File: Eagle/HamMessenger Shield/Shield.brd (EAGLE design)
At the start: 100 x 80 mm, 22 parts, among them J2 KEYBOARD GROVE, Q1 2N7000

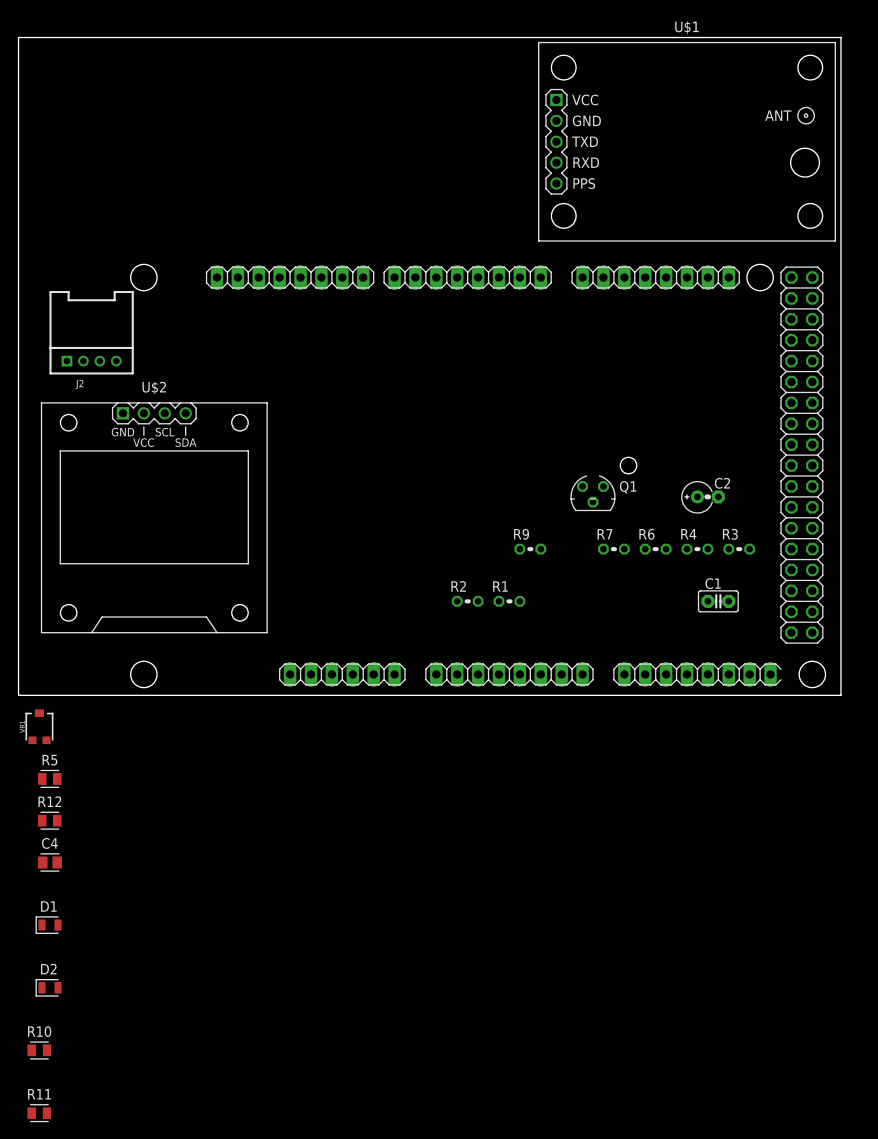
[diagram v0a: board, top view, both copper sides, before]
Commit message: Continue work on PCB. Update schematic.
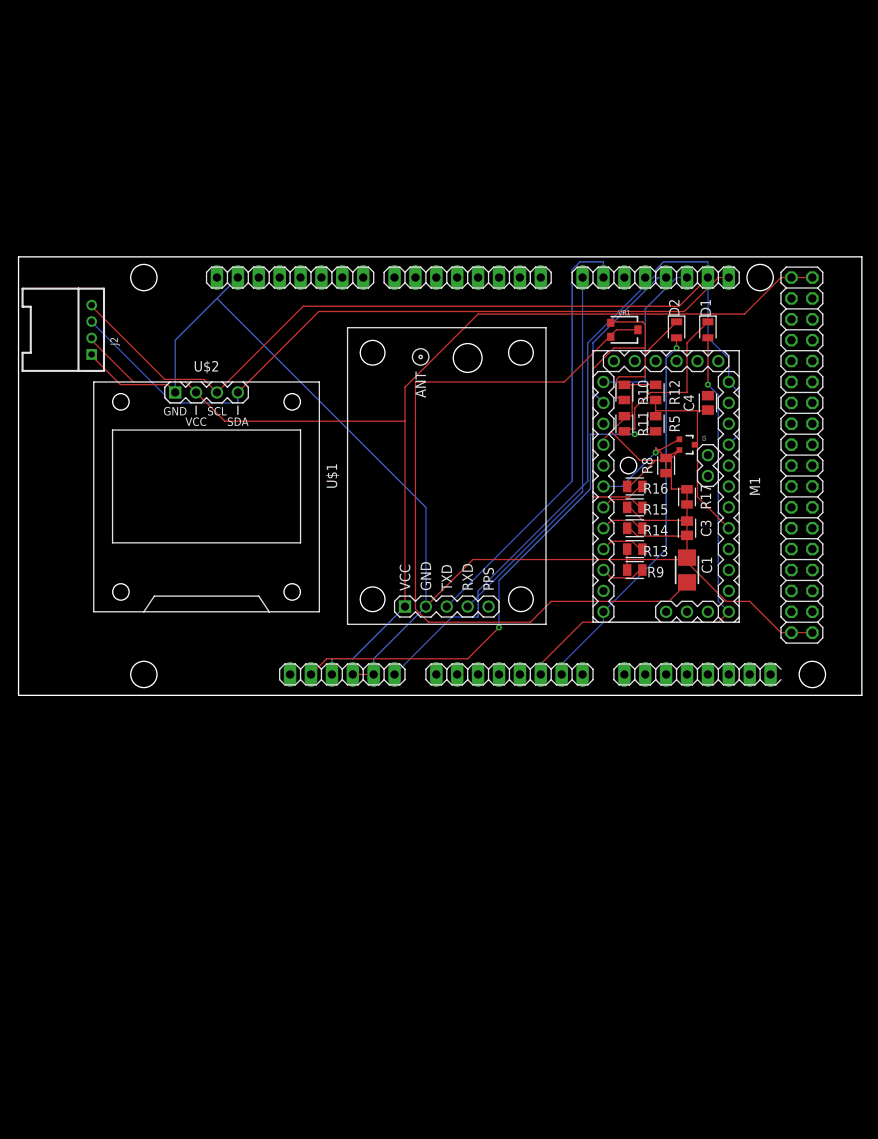
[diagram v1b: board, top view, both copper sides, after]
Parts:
- removed C2: 4.7uF, resistor:E2,5-4R
- removed Q1: 2N7000, transistor-fet-edited:TO92_MOD
- removed R1, R6: 1k, resistor:0204V
- removed R2: 2k2, resistor:0204V
- removed R3: 3k9, resistor:0204V
- removed R4: 8k2, resistor:0204V
- removed R7: 270, resistor:0204V
- added C3: 100nf, Capacitor:CAPC2012X110
- added M1: ARDUINO-PRO-MINI-3.3V, diy-modules:ARDUINO-PRO-MINI
- added Q3: MOSFET-NCHANNEL2N7002PW, BeagleBone_Blue_R3:SOT323
- added R13: 2k2, Resistor:RESC2012X65
- added R14: 3k9, Resistor:RESC2012X65
- added R15: 8k2, Resistor:RESC2012X65
- added R16: 1k, Resistor:RESC2012X65
- added R17: 270, Resistor:RESC2012X65
- added R8: 10k, Resistor:RESC2012X65
- C1: value 100nF -> 4.7uf; device capacitor-wima:C2.5-2 -> adafruit:CT3528
- R9: value 10k -> 1k; device rcl:0204V -> Resistor:RESC2012X65
- moved D2 110.5 mm to (80.0, 44.5), turned to 270 degrees
- moved R11 109.9 mm to (73.7, 33.0), turned to 270 degrees
- moved D1 107.9 mm to (83.8, 44.5), turned to 270 degrees
- moved R10 107.0 mm to (73.7, 36.8), turned to 270 degrees
- moved C4 97.6 mm to (83.8, 35.6), turned to 90 degrees
- moved R12 90.2 mm to (77.5, 36.8), turned to 270 degrees
- moved VR1 85.9 mm to (73.7, 44.5), turned to 270 degrees
- moved R5 85.4 mm to (77.5, 33.0), turned to 270 degrees
- moved U$1 50.0 mm to (52.1, 26.7), turned to 90 degrees
- moved R9 13.0 mm to (74.9, 15.2)
- moved U$2 6.84 mm to (22.9, 24.1)
- moved C1 5.39 mm to (81.3, 15.2), turned to 270 degrees
- moved J2 3.81 mm to (8.89, 44.5), turned to 90 degrees
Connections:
- removed net +VIN: IC1.6
- removed net RXD: U$1.4
- new net GND.2: M1.J6.2
- new net RX_GPS: IC1.29, U$1.3
- new net RX_MODEM: IC1.25, M1.J7.12
- new net TX_GPS: IC1.30, U$1.4
- new net TX_MODEM: IC1.26, M1.J7.11
- new net VCC: IC1.6, M1.J6.1, M1.J6.4
- net A0: now also M1.J6.8
- net D10: now also IC1.12, M1.J6.12
- net D3: now also M1.J7.7, Q3.1, R8.2; no longer Q1.2, R9.1
- net D4: now also M1.J7.6, R15.2; no longer R4.1
- net D5: now also M1.J7.5, R14.2; no longer R3.1
- net D6: now also M1.J7.4, R13.2; no longer R2.1
- net D7: now also M1.J7.3, R9.2; no longer R1.1
- net D9: now also IC1.13, M1.J7.1
- net GND: now also C1.-, C3.1, C3.2, M1.J7.9, Q3.2, R13.1, R14.1, R15.1, R16.1, R17.1, R17.2, R8.1, R9.1; no longer C1.1, C1.2, C2.-, Q1.3, R1.2, R2.2, R3.2, R4.2, R6.1, R7.1, R7.2, R9.2
- net LINE_LEVEL_OUT: now also C1.+; no longer C2.+
- net MIC_LEVEL_OUT: now also R16.2; no longer R6.2
- net PTT_V+: now also Q3.3; no longer Q1.1
- net SCL: now also IC1.24
- net SDA: now also IC1.23
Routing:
- net GND: track 0.00 -> 208.5 mm
- net +5V: track 0.00 -> 137.6 mm
- net VCC: track 0.00 -> 95.3 mm
- net LINE_LEVEL_OUT: track 0.00 -> 93.1 mm
- net SDA: track 0.00 -> 88.8 mm
- net SCL: track 0.00 -> 85.2 mm
- net +3V3: track 0.00 -> 61.4 mm, vias 0 -> 2
- net D10: track 0.00 -> 61.1 mm, vias 0 -> 1
- net RX_GPS: track 0.00 -> 53.4 mm
- net D9: track 0.00 -> 46.7 mm, vias 0 -> 1
- net TX_GPS: track 0.00 -> 45.8 mm
- net MIC_LEVEL_OUT: track 0.00 -> 36.7 mm
- net A0: track 0.00 -> 24.3 mm
- net N$4: track 0.00 -> 20.9 mm
- net RX_MODEM: track 0.00 -> 20.6 mm
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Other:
- board size 100 x 80 mm -> 102.5 x 53.3 mm

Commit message: Net re-routing
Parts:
- moved R8 1.27 mm to (78.7, 26.7)
- moved Q3 1.27 mm to (80.0, 30.5), turned to 0 degrees
- turned R16 to 180 degrees
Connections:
- new net N$2: C1.-, C3.1, R13.1, R14.1, R15.1, R17.2, R9.1
- net GND: no longer C1.-, C3.1, R13.1, R14.1, R15.1, R17.2, R9.1
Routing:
- net N$2: track 0.00 -> 21.8 mm
- net GND: track 208.5 -> 187.1 mm
- net MIC_LEVEL_OUT: track 36.7 -> 32.3 mm
- net VCC: track 95.3 -> 97.3 mm
- net D3: track 13.7 -> 15.3 mm
- net RX_MODEM: track 20.6 -> 19.9 mm
- net TX_MODEM: track 20.0 -> 19.4 mm

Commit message: PCB Updates
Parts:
- added J3: (no value), Wurth_Connectors_WR-TBL Rising Cage Clamp:691210910004
- moved R13 1.27 mm to (74.9, 16.5), turned to 180 degrees
- moved R14 1.27 mm to (74.9, 19.1), turned to 180 degrees
- moved R15 1.27 mm to (74.9, 21.6), turned to 180 degrees
- moved R9 1.27 mm to (74.9, 14.0), turned to 180 degrees
- moved R16 1.02 mm to (74.9, 24.4)
- turned R10 to 90 degrees
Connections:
- net GND: now also J3.1
- net LINE_LEVEL_IN: now also J3.4
- net MIC_LEVEL_OUT: now also J3.3
- net PTT_V+: now also J3.2
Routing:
- net LINE_LEVEL_IN: track 0.00 -> 121.8 mm, vias 0 -> 4
- net PTT_V+: track 0.00 -> 96.9 mm, vias 0 -> 3
- net MIC_LEVEL_OUT: track 32.3 -> 121.2 mm, vias 0 -> 4
- net VCC: track 97.3 -> 82.2 mm, vias 0 -> 2
- net GND: track 187.1 -> 181.6 mm
- net RX_GPS: track 53.4 -> 48.9 mm, vias 0 -> 1
- net N$3: track 15.4 -> 11.2 mm
- net D9: track 46.7 -> 50.4 mm
- net D7: track 5.52 -> 3.42 mm
- net D6: track 5.52 -> 3.42 mm
- net D5: track 5.52 -> 3.42 mm
- net D4: track 5.52 -> 3.42 mm
- net +3V3: track 61.4 -> 62.7 mm
- net N$2: track 21.8 -> 22.9 mm
- net SDA: track 88.8 -> 89.7 mm, vias 0 -> 1
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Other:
- board size 102.5 x 53.3 mm -> 101.6 x 53.3 mm

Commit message: Add ground plane
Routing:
- net MIC_LEVEL_OUT: track 121.2 -> 118.0 mm
- net GND: vias 0 -> 6
- added copper zone on layer 1, net GND
- added copper zone on layer 16, net GND
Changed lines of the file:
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@@
 <wire x1="17.78" y1="21.844" x2="45.974" y2="21.844" width="0.1524" layer="16"/>
 <via x="45.974" y="21.844" extent="1-16" drill="0.35"/>
-<wire x1="45.974" y1="21.844" x2="45.974" y2="29.972" width="0.1524" layer="1"/>
-<via x="45.974" y="29.972" extent="1-16" drill="0.35"/>
-<wire x1="45.974" y1="29.972" x2="65.532" y2="29.972" width="0.1524" layer="16"/>
-<via x="65.532" y="29.972" extent="1-16" drill="0.35"/>
-<wire x1="65.532" y1="29.972" x2="68.834" y2="26.67" width="0.1524" layer="1"/>
-<wire x1="68.834" y1="26.67" x2="68.834" y2="23.114" width="0.1524" layer="1"/>
+<wire x1="45.974" y1="21.844" x2="45.974" y2="28.194" width="0.1524" layer="1"/>
+<via x="45.974" y="28.194" extent="1-16" drill="0.35"/>
+<wire x1="65.278" y1="28.194" x2="45.974" y2="28.194" width="0.1524" layer="16"/>
+<wire x1="65.278" y1="28.194" x2="65.532" y2="28.448" width="0.1524" layer="16"/>
+<via x="65.532" y="28.448" extent="1-16" drill="0.35"/>
+<wire x1="65.532" y1="28.448" x2="68.834" y2="25.146" width="0.1524" layer="1"/>
+<wire x1="68.834" y1="25.146" x2="68.834" y2="23.114" width="0.1524" layer="1"/>
 <via x="68.834" y="23.114" extent="1-16" drill="0.35"/>
 <wire x1="68.834" y1="23.114" x2="70.104" y2="24.384" width="0.1524" layer="16"/>
@@
 <wire x1="4.572" y1="13.716" x2="19.05" y2="28.194" width="0.1524" layer="1"/>
 <wire x1="19.05" y1="28.194" x2="19.05" y2="36.83" width="0.1524" layer="1"/>
-<wire x1="81.28" y1="19.6723" x2="81.28" y2="19.4446" width="0" layer="19" extent="1-1"/>
-<wire x1="49.53" y1="10.795" x2="71.12" y2="30.48" width="0" layer="19" extent="1-1"/>
+<polygon width="0.1524" layer="1" isolate="0.4064">
+<vertex x="0" y="53.34"/>
+<vertex x="0" y="0"/>
+<vertex x="101.6" y="0"/>
+<vertex x="101.6" y="53.34"/>
+</polygon>
+<polygon width="0.1524" layer="16" isolate="0.4064">
+<vertex x="0" y="53.34"/>
+<vertex x="101.6" y="53.34"/>
+<vertex x="101.6" y="0"/>
+<vertex x="0" y="0"/>
+</polygon>
+<via x="38.608" y="41.148" extent="1-16" drill="0.35"/>
+<via x="65.786" y="42.418" extent="1-16" drill="0.35"/>
+<via x="65.024" y="14.732" extent="1-16" drill="0.35"/>
+<via x="66.04" y="8.636" extent="1-16" drill="0.35"/>
+<via x="74.93" y="10.16" extent="1-16" drill="0.35"/>
+<via x="80.518" y="35.814" extent="1-16" drill="0.35"/>
 </signal>
 <signal name="D3">
@@
 <contactref element="U$1" pad="1"/>
 <contactref element="U$2" pad="2"/>
-<wire x1="13.97" y1="38.1" x2="8.89" y2="43.18" width="0.1524" layer="1"/>
-<wire x1="20.32" y1="38.1" x2="13.97" y2="38.1" width="0.1524" layer="1"/>
-<wire x1="21.59" y1="36.83" x2="20.32" y2="38.1" width="0.1524" layer="1"/>
+<wire x1="13.716" y1="38.354" x2="8.89" y2="43.18" width="0.1524" layer="1"/>
+<wire x1="20.066" y1="38.354" x2="13.716" y2="38.354" width="0.1524" layer="1"/>
+<wire x1="21.59" y1="36.83" x2="20.066" y2="38.354" width="0.1524" layer="1"/>
 <wire x1="8.89" y1="43.18" x2="8.89" y2="43.45" width="0.1524" layer="1"/>
 <wire x1="96.52" y1="50.8" x2="93.98" y2="50.8" width="0.1524" layer="1"/>
@@
 <contactref element="U$2" pad="3"/>
 <contactref element="IC1" pad="24"/>
-<wire x1="17.78" y1="38.4175" x2="8.89" y2="47.3075" width="0.1524" layer="1"/>
-<wire x1="22.5425" y1="38.4175" x2="17.78" y2="38.4175" width="0.1524" layer="1"/>
-<wire x1="24.13" y1="36.83" x2="22.5425" y2="38.4175" width="0.1524" layer="1"/>
-<wire x1="8.89" y1="47.3075" x2="8.89" y2="47.45" width="0.1524" layer="1"/>
+<wire x1="8.89" y1="47.45" x2="11.0335" y2="47.45" width="0.1524" layer="1"/>
+<wire x1="18.034" y1="40.4495" x2="11.0335" y2="47.45" width="0.1524" layer="1"/>
+<wire x1="20.5105" y1="40.4495" x2="18.034" y2="40.4495" width="0.1524" layer="1"/>
+<wire x1="24.13" y1="36.83" x2="20.5105" y2="40.4495" width="0.1524" layer="1"/>
 <wire x1="24.13" y1="36.83" x2="34.544" y2="47.244" width="0.1524" layer="1"/>
 <wire x1="34.544" y1="47.244" x2="79.756" y2="47.244" width="0.1524" layer="1"/>
@@
 <wire x1="85.09" y1="11.43" x2="85.09" y2="36.5125" width="0.1524" layer="16"/>
 <wire x1="86.36" y1="10.16" x2="85.09" y2="11.43" width="0.1524" layer="16"/>
-<wire x1="68.58" y1="8.89" x2="63.5" y2="3.81" width="0.1524" layer="1"/>
-<wire x1="63.5" y1="3.81" x2="63.5" y2="2.54" width="0.1524" layer="1"/>
-<wire x1="85.09" y1="8.89" x2="68.58" y2="8.89" width="0.1524" layer="1"/>
+<wire x1="68.072" y1="8.89" x2="63.5" y2="4.318" width="0.1524" layer="1"/>
+<wire x1="63.5" y1="4.318" x2="63.5" y2="2.54" width="0.1524" layer="1"/>
+<wire x1="85.09" y1="8.89" x2="68.072" y2="8.89" width="0.1524" layer="1"/>
 <wire x1="86.36" y1="10.16" x2="85.09" y2="8.89" width="0.1524" layer="1"/>
 <via x="83.82" y="37.7825" extent="1-16" drill="0.35"/>

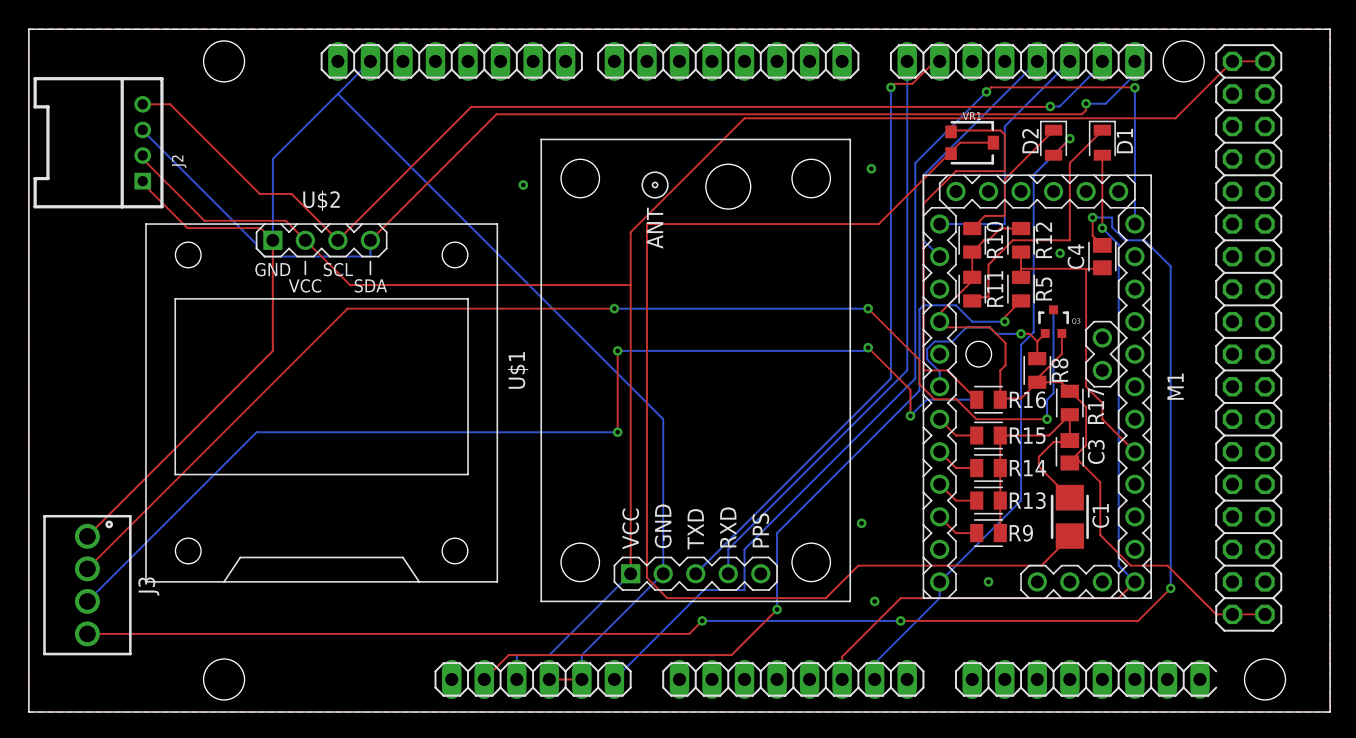
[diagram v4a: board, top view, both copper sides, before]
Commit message: add SD card. rerouting.
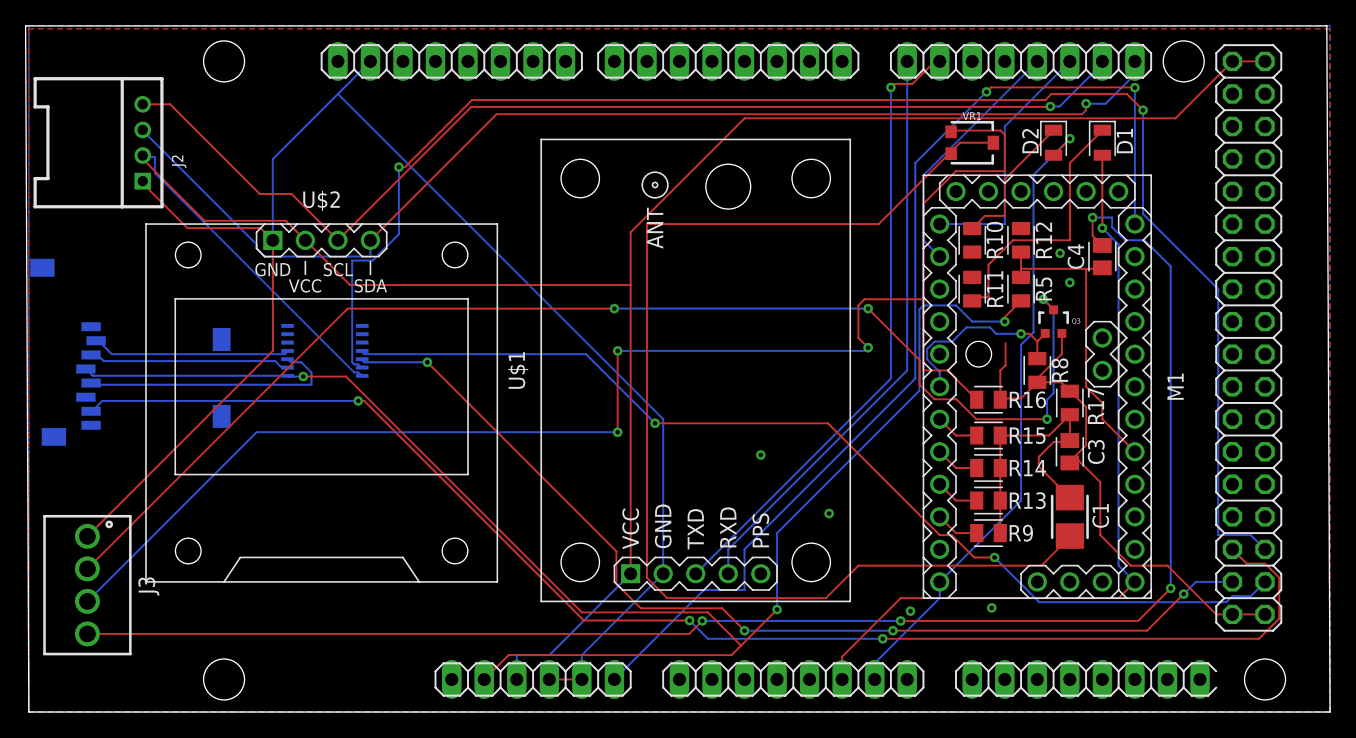
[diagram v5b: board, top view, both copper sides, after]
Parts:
- added U$3: MICROSD, adafruit:MICROSD
- added U2: (no value), adafruit:TSSOP14
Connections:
- removed net GND.2: M1.J6.2
- new net MISO: IC1.77, U$3.7
- new net MOSI: IC1.78, U2.13
- new net N$1: U$3.3, U2.2
- new net N$5: U$3.5, U2.3
- new net N$6: U$3.2, U2.4
- new net SCK: IC1.79, U2.12
- new net SS: IC1.80, U2.11
- net +3V3: now also U$3.4, U2.1
- net +5V: now also U2.14
- net GND: now also M1.J6.2, U$3.MT1, U$3.MT2, U2.7
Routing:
- net MOSI: track 0.00 -> 119.3 mm, vias 0 -> 2
- net MISO: track 0.00 -> 109.2 mm, vias 0 -> 3
- net SCK: track 0.00 -> 79.8 mm, vias 0 -> 4
- net SS: track 0.00 -> 79.3 mm, vias 0 -> 2
- net +3V3: track 62.7 -> 122.7 mm, vias 2 -> 3
- net +5V: track 137.6 -> 162.7 mm
- net N$5: track 0.00 -> 20.5 mm
- net GND: track 181.6 -> 164.7 mm
- net N$1: track 0.00 -> 15.8 mm
- net N$6: track 0.00 -> 15.5 mm
- net MIC_LEVEL_OUT: track 118.0 -> 114.5 mm, vias 4 -> 3
- net PTT_V+: track 96.9 -> 99.1 mm, vias 3 -> 4
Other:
- board size 101.6 x 53.3 mm -> 101.9 x 53.6 mm
